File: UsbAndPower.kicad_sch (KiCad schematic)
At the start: 16 parts, among them J4 USB_C_Receptacle_USB2.0_16P, Q4 ZXMN3A14F, Q6 DMG2301L, U4 LM1117MP-3.3, U5 HT75xx-1-SOT89

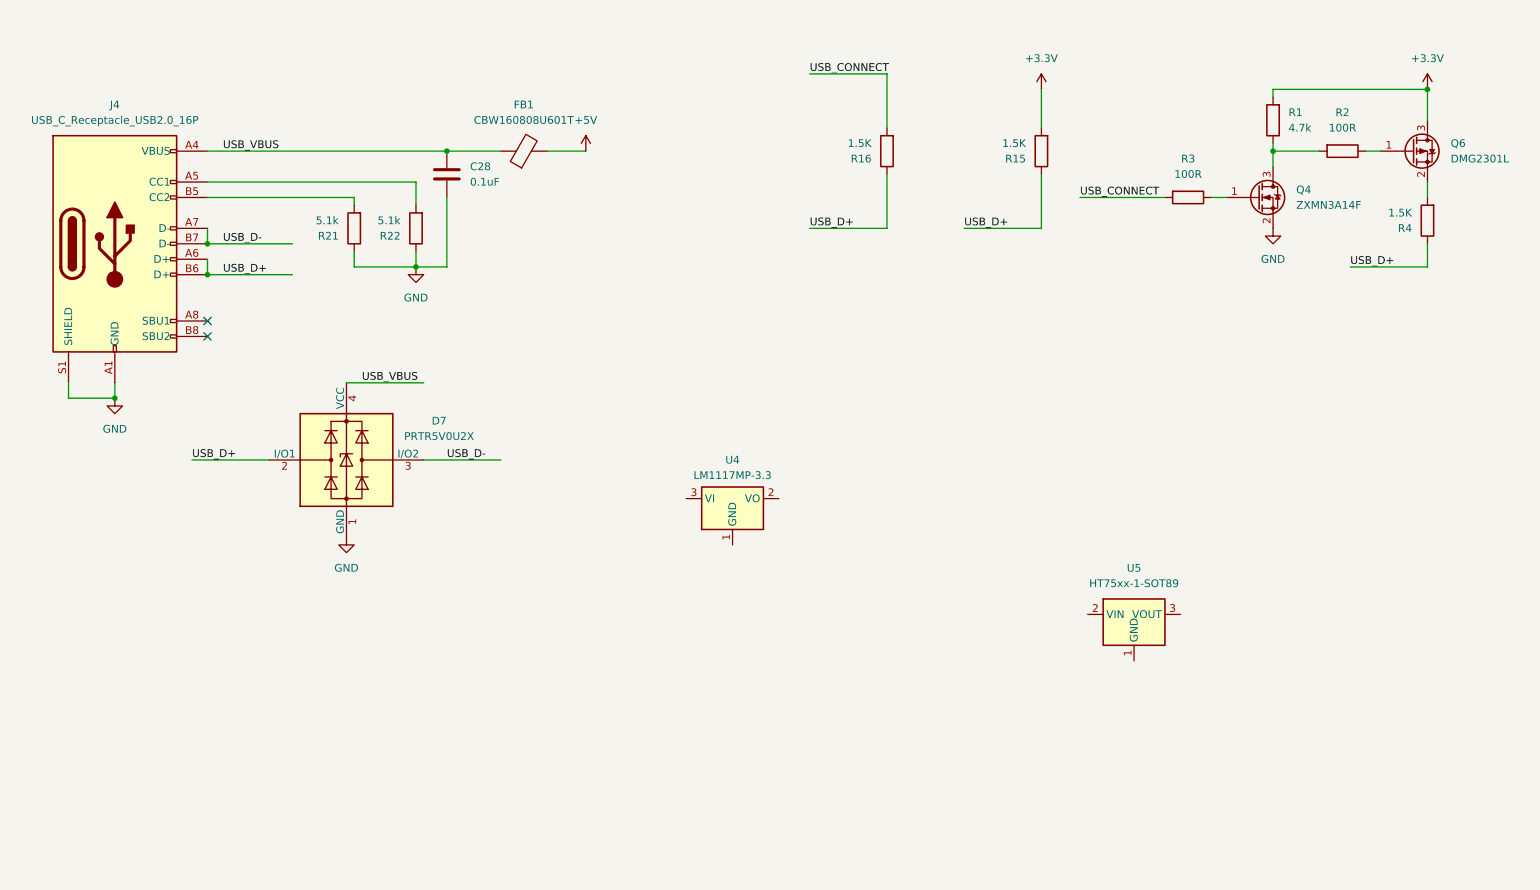
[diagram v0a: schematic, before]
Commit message: 3.3v power ok
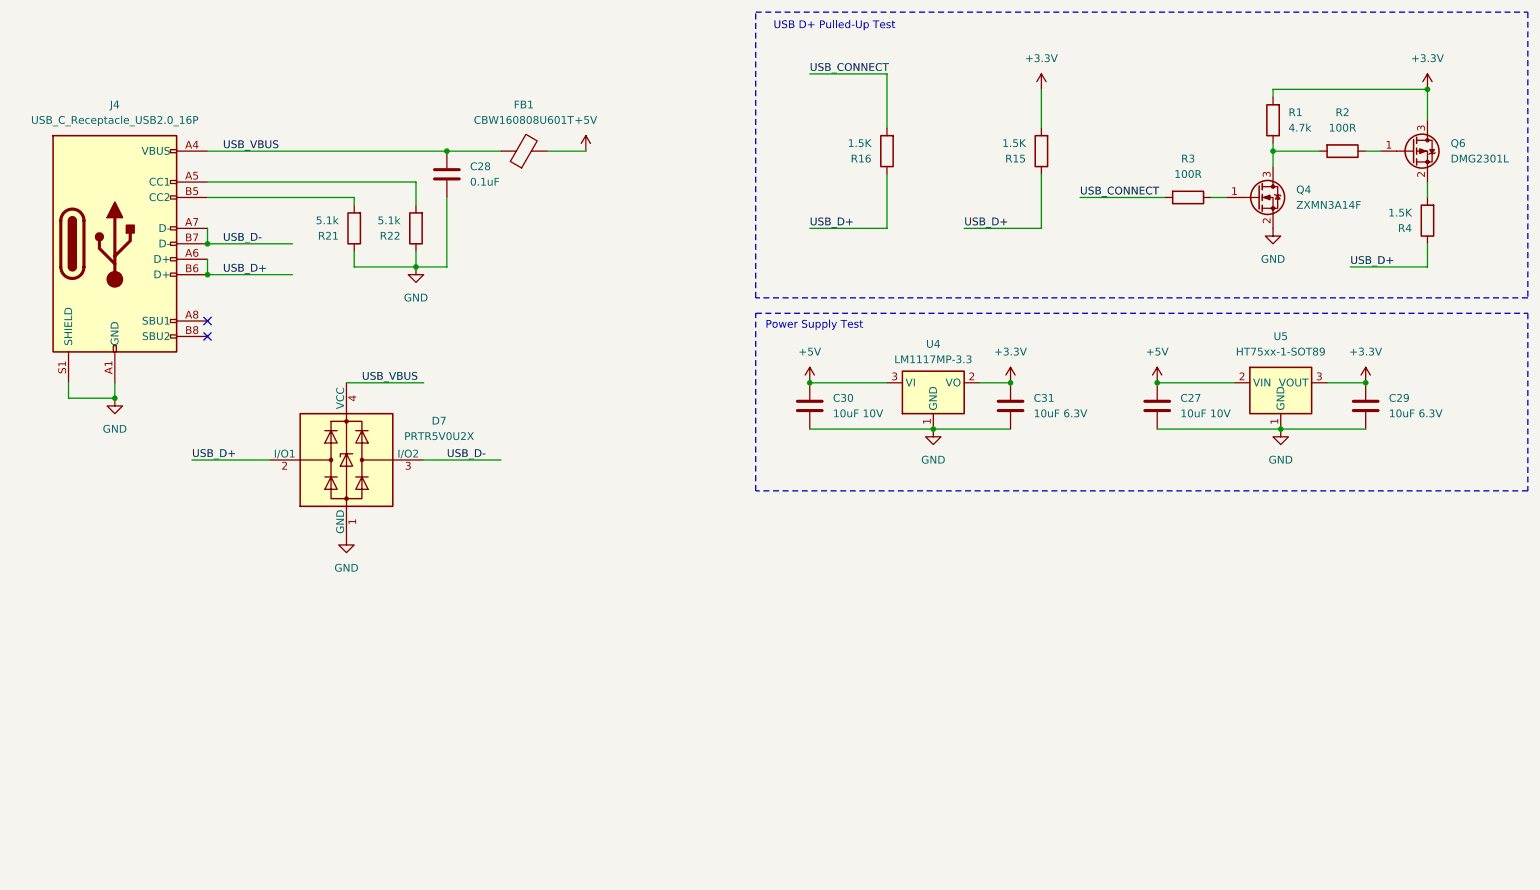
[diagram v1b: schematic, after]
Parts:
- added C27, C30: 10uF 10V, Capacitor_SMD:C_0805_2012Metric, symbol Device:C
- added C29, C31: 10uF 6.3V, Capacitor_SMD:C_0805_2012Metric, symbol Device:C
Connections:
- net +3.3V: now also U4.2 (VO), U5.3 (VOUT), C29.1, C31.1
- net +5V: now also U4.3 (VI), U5.2 (VIN), C27.1, C30.1
- net GND: now also U4.1 (GND), U5.1 (GND), C27.2, C29.2, C30.2, C31.2
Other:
- note added: "Power Supply Test"
- note added: "USB D+ Pulled-Up Test"
- moved on the sheet: U4, U5

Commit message: temp
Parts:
- added C32: 10uF 10V, Capacitor_SMD:C_0805_2012Metric, symbol Device:C
- added U6: RT9193-18GB, Package_TO_SOT_SMD:SOT-23-5, symbol Regulator_Linear:AP131-18
- added U7: RT9193-33GB, Package_TO_SOT_SMD:SOT-23-5, symbol Regulator_Linear:AP131-33
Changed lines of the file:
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@@
+	)
+	(symbol
+		(lib_id "Device:C")
+		(at 147.32 118.11 0)
+		(unit 1)
+		(exclude_from_sim no)
+		(in_bom yes)
+		(on_board yes)
+		(dnp no)
+		(fields_autoplaced yes)
+		(property "Reference" "C32"
+			(at 151.13 116.8399 0)
+			(effects
+				(font
+					(size 1.27 1.27)
+				)
+				(justify left)
+			)
+		)
+		(property "Value" "10uF 10V"
+			(at 151.13 119.3799 0)
+			(effects
+				(font
+					(size 1.27 1.27)
+				)
+				(justify left)
+			)
+		)
+		(property "Footprint" "Capacitor_SMD:C_0805_2012Metric"
+			(at 148.2852 121.92 0)
+			(effects
+				(font
+					(size 1.27 1.27)
+				)
+				(hide yes)
+			)
+		)
+		(property "Datasheet" "~"
+			(at 147.32 118.11 0)
+			(effects
+				(font
+					(size 1.27 1.27)
+				)
+				(hide yes)
+			)
+		)
+		(property "Description" "Unpolarized capacitor"
+			(at 147.32 118.11 0)
+			(effects
+				(font
+					(size 1.27 1.27)
+				)
+				(hide yes)
+			)
+		)
+		(pin "2"
+		)
+		(pin "1"
+		)
+		(instances
+			(project "DapLink_STM32F103CBT6"
+				(path "/62d13f52-5b95-4b2e-9bc7-6f5f907932ec/a477e6ea-0fc3-4cc5-9f90-9fe3a9e18e1a"
+					(reference "C32")
+					(unit 1)
+				)
+			)
+		)
 	)
 	(symbol
@@
 	)
 	(symbol
+		(lib_id "Regulator_Linear:AP131-33")
+		(at 227.33 119.38 0)
+		(unit 1)
+		(exclude_from_sim no)
+		(in_bom yes)
+		(on_board yes)
+		(dnp no)
+		(fields_autoplaced yes)
+		(property "Reference" "U7"
+			(at 227.33 110.49 0)
+			(effects
+				(font
+					(size 1.27 1.27)
+				)
+			)
+		)
+		(property "Value" "RT9193-33GB"
+			(at 227.33 113.03 0)
+			(effects
+				(font
+					(size 1.27 1.27)
+				)
+			)
+		)
+		(property "Footprint" "Package_TO_SOT_SMD:SOT-23-5"
+			(at 227.33 111.125 0)
+			(effects
+				(font
+					(size 1.27 1.27)
+				)
+				(hide yes)
+			)
+		)
+		(property "Datasheet" "https://www.richtek.com/assets/product_file/RT9193/DS9193-18.pdf"
+			(at 227.33 119.38 0)
+			(effects
+				(font
+					(size 1.27 1.27)
+				)
+				(hide yes)
+			)
+		)
+		(property "Description" "300mA, Ultra-Low Noise, Ultra-Fast CMOS LDO Regulator, shutdown pin, 3.3V fixed positive output, SOT-23-5"
+			(at 227.33 119.38 0)
+			(effects
+				(font
+					(size 1.27 1.27)
+				)
+				(hide yes)
+			)
+		)
+		(pin "3"
+		)
+		(pin "1"
+		)
+		(pin "4"
+		)
+		(pin "2"
+		)
+		(pin "5"
+		)
+		(instances
+			(project ""
+				(path "/62d13f52-5b95-4b2e-9bc7-6f5f907932ec/a477e6ea-0fc3-4cc5-9f90-9fe3a9e18e1a"
+					(reference "U7")
+					(unit 1)
+				)
+			)
+		)
+	)
+	(symbol
 		(lib_name "GND_1")
 		(lib_id "power:GND")
@@
 					(unit 1)
 				)
+			)
+		)
+	)
+	(symbol
+		(lib_id "Regulator_Linear:AP131-18")
+		(at 175.26 118.11 0)
+		(unit 1)
+		(exclude_from_sim no)
+		(in_bom yes)
+		(on_board yes)
+		(dnp no)
+		(fields_autoplaced yes)
+		(property "Reference" "U6"
+			(at 175.26 109.22 0)
+			(effects
+				(font
+					(size 1.27 1.27)
+				)
+			)
+		)
+		(property "Value" "RT9193-18GB"
+			(at 175.26 111.76 0)
+			(effects
+				(font
+					(size 1.27 1.27)
+				)
+			)
+		)
+		(property "Footprint" "Package_TO_SOT_SMD:SOT-23-5"
+			(at 175.26 109.855 0)
+			(effects
+				(font
+					(size 1.27 1.27)
+				)
+				(hide yes)
+			)
+		)
+		(property "Datasheet" "https://www.richtek.com/assets/product_file/RT9193/DS9193-18.pdf"
+			(at 175.26 118.11 0)
+			(effects
+				(font
+					(size 1.27 1.27)
+				)
+				(hide yes)
+			)
+		)
+		(property "Description" "300mA, Ultra-Low Noise, Ultra-Fast CMOS LDO Regulator, shutdown pin, 1.8V fixed positive output, SOT-23-5"
+			(at 175.26 118.11 0)
+			(effects
+				(font
+					(size 1.27 1.27)
+				)
+				(hide yes)
+			)
+		)
+		(pin "3"
+		)
+		(pin "4"
+		)
+		(pin "2"
+		)
+		(pin "5"
+		)
+		(pin "1"
+		)
+		(instances
+			(project ""
+				(path "/62d13f52-5b95-4b2e-9bc7-6f5f907932ec/a477e6ea-0fc3-4cc5-9f90-9fe3a9e18e1a"
+					(reference "U6")
+					(unit 1)
+				)

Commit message: temp power
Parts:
- added C33, C35, C37: 1uF 10V X7R, Capacitor_SMD:C_0805_2012Metric, symbol Device:C
- added C34, C36: 22nF, Capacitor_SMD:C_0805_2012Metric, symbol Device:C
- C32: value 10uF 10V -> 1uF 10V X7R
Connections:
- net +3.3V: now also U7.5 (OUT), C37.1
- net +5V: now also C32.1, U6.1 (IN), U6.3 (EN), U7.1 (IN), U7.3 (EN), C35.1
- net GND: now also C32.2, U6.2 (GND), U7.2 (GND), C33.2, C34.2, C35.2, C36.2, C37.2
- net at U7.4 (BP): now also C36.1
- net at U6.4 (BP): now also C34.1
- net +1.8V: now reaches U6.5 (OUT)
- net +1.8V: now also C33.1
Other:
- note added: "Power Supply Test 3.3V"
- note removed: "Power Supply Test"
- moved on the sheet: C32, U6, U7

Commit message: temp
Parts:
- C32, C33, C35, C37: footprint Capacitor_SMD:C_0805_2012Metric -> Capacitor_SMD:C_1206_3216Metric
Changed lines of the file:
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@@
 			)
 		)
-		(property "Footprint" "Capacitor_SMD:C_0805_2012Metric"
+		(property "Footprint" "Capacitor_SMD:C_1206_3216Metric"
 			(at 215.5952 116.84 0)
 			(effects
@@
 			)
 		)
-		(property "Footprint" "Capacitor_SMD:C_0805_2012Metric"
+		(property "Footprint" "Capacitor_SMD:C_1206_3216Metric"
 			(at 215.5952 146.05 0)
 			(effects
@@
 			)
 		)
-		(property "Footprint" "Capacitor_SMD:C_0805_2012Metric"
+		(property "Footprint" "Capacitor_SMD:C_1206_3216Metric"
 			(at 166.0652 116.84 0)
 			(effects
@@
 			)
 		)
-		(property "Footprint" "Capacitor_SMD:C_0805_2012Metric"
+		(property "Footprint" "Capacitor_SMD:C_1206_3216Metric"
 			(at 166.0652 146.05 0)
 			(effects

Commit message: temp
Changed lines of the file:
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@@
-	(wire
-		(pts
-			(xy 80.01 58.42) (xy 66.04 58.42)
-		)
-		(stroke
-			(width 0)
-			(type default)
-		)
-	)
 	(wire
 		(pts
@@
 	(wire
 		(pts
+			(xy 66.04 58.42) (xy 69.85 58.42)
+		)
+		(stroke
+			(width 0)
+			(type default)
+		)
+	)
+	(wire
+		(pts
 			(xy 214.63 116.84) (xy 214.63 121.92)
 		)
@@
 	(wire
 		(pts
-			(xy 80.01 53.34) (xy 66.04 53.34)
-		)
-		(stroke
-			(width 0)
-			(type default)
-		)
-	)
-	(wire
-		(pts
 			(xy 63.5 88.9) (xy 76.2 88.9)
 		)
@@
 		(pts
 			(xy 250.19 76.2) (xy 256.54 76.2)
+		)
+		(stroke
+			(width 0)
+			(type default)
+		)
+	)
+	(wire
+		(pts
+			(xy 66.04 53.34) (xy 69.85 53.34)
 		)
 		(stroke
@@
 		)
 	)
-	(label "USB_D+"
-		(at 68.58 58.42 0)
-		(fields_autoplaced yes)
-		(effects
-			(font
-				(size 1.27 1.27)
-			)
-			(justify left bottom)
-		)
-	)
 	(label "USB_CONNECT"
 		(at 165.1 25.4 0)
@@
 		)
 	)
-	(label "USB_D-"
-		(at 68.58 53.34 0)
-		(fields_autoplaced yes)
-		(effects
-			(font
-				(size 1.27 1.27)
-			)
-			(justify left bottom)
-		)
-	)
 	(label "USB_VBUS"
 		(at 91.44 76.2 0)
@@
 		)
 	)
+	(hierarchical_label "USB_D-"
+		(shape bidirectional)
+		(at 69.85 53.34 0)
+		(fields_autoplaced yes)
+		(effects
+			(font
+				(size 1.27 1.27)
+			)
+			(justify left)
+		)
+	)
+	(hierarchical_label "USB_D+"
+		(shape bidirectional)
+		(at 69.85 58.42 0)
+		(fields_autoplaced yes)
+		(effects
+			(font
+				(size 1.27 1.27)
+			)
+			(justify left)
+		)
+	)

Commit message: temp
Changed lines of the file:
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@@
 	(wire
 		(pts
-			(xy 209.55 45.72) (xy 223.52 45.72)
+			(xy 220.98 45.72) (xy 223.52 45.72)
 		)
 		(stroke
@@
 		)
 	)
-	(label "USB_CONNECT"
-		(at 209.55 45.72 0)
-		(fields_autoplaced yes)
-		(effects
-			(font
-				(size 1.27 1.27)
-			)
-			(justify left bottom)
-		)
-	)
 	(label "USB_D-"
 		(at 105.41 88.9 0)
@@
 		)
 	)
+	(hierarchical_label "USB_CONNECT"
+		(shape input)
+		(at 220.98 45.72 180)
+		(fields_autoplaced yes)
+		(effects
+			(font
+				(size 1.27 1.27)
+			)
+			(justify right)
+		)
+	)

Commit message: temp
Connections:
- net +3.3V: now also Q6.2 (S); no longer C37.1, Q6.3 (D), U7.5 (OUT)
- net at R4.2: now also Q6.3 (D); no longer Q6.2 (S)
- net +1.8V renamed +1.8V_LDO
- new net +3.3V_LDO: C37.1, U7.5 (OUT)
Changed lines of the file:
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@@
+	(wire
+		(pts
+			(xy 177.8 27.94) (xy 177.8 34.29)
+		)
+		(stroke
+			(width 0)
+			(type default)
+		)
+	)
 	(wire
 		(pts
@@
 	(wire
 		(pts
+			(xy 165.1 27.94) (xy 177.8 27.94)
+		)
+		(stroke
+			(width 0)
+			(type default)
+		)
+	)
+	(wire
+		(pts
 			(xy 165.1 121.92) (xy 193.04 121.92)
 		)
@@
 	(wire
 		(pts
-			(xy 165.1 25.4) (xy 177.8 25.4)
-		)
-		(stroke
-			(width 0)
-			(type default)
-		)
-	)
-	(wire
-		(pts
 			(xy 250.19 76.2) (xy 256.54 76.2)
 		)
@@
 	(wire
 		(pts
-			(xy 177.8 25.4) (xy 177.8 34.29)
-		)
-		(stroke
-			(width 0)
-			(type default)
-		)
-	)
-	(wire
-		(pts
 			(xy 241.3 27.94) (xy 266.7 27.94)
 		)
@@
 	(wire
 		(pts
-			(xy 121.92 38.1) (xy 128.27 38.1)
+			(xy 121.92 38.1) (xy 130.81 38.1)
 		)
 		(stroke
@@
 		)
 	)
-	(label "USB_D+"
-		(at 63.5 88.9 0)
+	(label "USB_CONNECT"
+		(at 165.1 27.94 0)
 		(fields_autoplaced yes)
 		(effects
@@
 		)
 	)
-	(label "USB_D-"
-		(at 105.41 88.9 0)
+	(label "USB_D+"
+		(at 63.5 88.9 0)
 		(fields_autoplaced yes)
 		(effects
@@
 		)
 	)
-	(label "USB_CONNECT"
-		(at 165.1 25.4 0)
+	(label "USB_D-"
+		(at 105.41 88.9 0)
 		(fields_autoplaced yes)
 		(effects
@@
 			)
 		)
-		(property "Value" "+3.3V"
+		(property "Value" "+3.3V_LDO"
 			(at 214.63 133.35 0)
 			(effects
@@
 		(on_board yes)
 		(dnp no)
-		(fields_autoplaced yes)
 		(property "Reference" "FB1"
 			(at 118.0592 30.48 90)
@@
 		(lib_id "Transistor_FET:DMG2301L")
 		(at 264.16 38.1 0)
-		(unit 1)
-		(exclude_from_sim no)
-		(in_bom yes)
-		(on_board yes)
-		(dnp no)
-		(fields_autoplaced yes)
+		(mirror x)
+		(unit 1)
+		(exclude_from_sim no)
+		(in_bom yes)
+		(on_board yes)
+		(dnp no)
 		(property "Reference" "Q6"
-			(at 270.51 36.8299 0)
+			(at 270.51 39.3701 0)
 			(effects
 				(font
@@
 		)
 		(property "Value" "DMG2301L"
-			(at 270.51 39.3699 0)
+			(at 270.51 36.8301 0)
 			(effects
 				(font
@@
 		)
 		(property "Footprint" "Package_TO_SOT_SMD:SOT-23"
-			(at 269.24 40.005 0)
+			(at 269.24 36.195 0)
 			(effects
 				(font
@@
 		)
 		(property "Datasheet" "https://www.diodes.com/assets/Datasheets/DMG2301L.pdf"
-			(at 269.24 41.91 0)
+			(at 269.24 34.29 0)
 			(effects
 				(font
@@
 	(symbol
 		(lib_id "power:+5V")
-		(at 128.27 38.1 0)
+		(at 130.81 38.1 0)
 		(unit 1)
 		(exclude_from_sim no)
@@
 		(fields_autoplaced yes)
 		(property "Reference" "#PWR071"
-			(at 128.27 41.91 0)
+			(at 130.81 41.91 0)
 			(effects
 				(font
@@
 		)
 		(property "Value" "+5V"
-			(at 128.27 33.02 0)
+			(at 130.81 33.02 0)
 			(effects
 				(font
@@
 		)
 		(property "Footprint" ""
-			(at 128.27 38.1 0)
+			(at 130.81 38.1 0)
 			(effects
 				(font
@@
 		)
 		(property "Datasheet" ""
-			(at 128.27 38.1 0)
+			(at 130.81 38.1 0)
 			(effects
 				(font
@@
 		)
 		(property "Description" "Power symbol creates a global label with name \"+5V\""
-			(at 128.27 38.1 0)
+			(at 130.81 38.1 0)
 			(effects
 				(font
@@
 			)
 		)
-		(property "Value" "+1.8V"
+		(property "Value" "+1.8V_LDO"
 			(at 214.63 104.14 0)
 			(effects

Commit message: temp
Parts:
- removed Q6: DMG2301L, Package_TO_SOT_SMD:SOT-23, symbol Transistor_FET:DMG2301L
- added Q5: SI2301, Package_TO_SOT_SMD:SOT-23, symbol Transistor_FET:DMG2301L
- Q4: value ZXMN3A14F -> SI2306
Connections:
- net +3.3V: now also Q5.2 (S)
- net at R2.1: now also Q5.1 (G)
- net at R4.2: now also Q5.3 (D)
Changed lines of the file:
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@@
+	)
+	(symbol
+		(lib_id "Transistor_FET:DMG2301L")
+		(at 264.16 38.1 0)
+		(mirror x)
+		(unit 1)
+		(exclude_from_sim no)
+		(in_bom yes)
+		(on_board yes)
+		(dnp no)
+		(property "Reference" "Q5"
+			(at 270.51 39.3701 0)
+			(effects
+				(font
+					(size 1.27 1.27)
+				)
+				(justify left)
+			)
+		)
+		(property "Value" "SI2301"
+			(at 270.51 36.8301 0)
+			(effects
+				(font
+					(size 1.27 1.27)
+				)
+				(justify left)
+			)
+		)
+		(property "Footprint" "Package_TO_SOT_SMD:SOT-23"
+			(at 269.24 36.195 0)
+			(effects
+				(font
+					(size 1.27 1.27)
+					(italic yes)
+				)
+				(justify left)
+				(hide yes)
+			)
+		)
+		(property "Datasheet" "https://www.mccsemi.com/pdf/Products/SI2301(SOT-23).pdf"
+			(at 269.24 34.29 0)
+			(effects
+				(font
+					(size 1.27 1.27)
+				)
+				(justify left)
+				(hide yes)
+			)
+		)
+		(property "Description" "-2.8A Id, -20V Vds, +-8V Vgs, Rds 50mR, P-Channel MOSFET, SOT-23"
+			(at 264.16 38.1 0)
+			(effects
+				(font
+					(size 1.27 1.27)
+				)
+				(hide yes)
+			)
+		)
+		(pin "2"
+		)
+		(pin "1"
+		)
+		(pin "3"
+		)
+		(instances
+			(project "DapLink_STM32F103CBT6"
+				(path "/62d13f52-5b95-4b2e-9bc7-6f5f907932ec/a477e6ea-0fc3-4cc5-9f90-9fe3a9e18e1a"
+					(reference "Q5")
+					(unit 1)
+				)
+			)
+		)
 	)
 	(symbol
@@
 	)
 	(symbol
-		(lib_id "Transistor_FET:DMG2301L")
-		(at 264.16 38.1 0)
-		(mirror x)
-		(unit 1)
-		(exclude_from_sim no)
-		(in_bom yes)
-		(on_board yes)
-		(dnp no)
-		(property "Reference" "Q6"
-			(at 270.51 39.3701 0)
-			(effects
-				(font
-					(size 1.27 1.27)
-				)
-				(justify left)
-			)
-		)
-		(property "Value" "DMG2301L"
-			(at 270.51 36.8301 0)
-			(effects
-				(font
-					(size 1.27 1.27)
-				)
-				(justify left)
-			)
-		)
-		(property "Footprint" "Package_TO_SOT_SMD:SOT-23"
-			(at 269.24 36.195 0)
-			(effects
-				(font
-					(size 1.27 1.27)
-					(italic yes)
-				)
-				(justify left)
-				(hide yes)
-			)
-		)
-		(property "Datasheet" "https://www.diodes.com/assets/Datasheets/DMG2301L.pdf"
-			(at 269.24 34.29 0)
-			(effects
-				(font
-					(size 1.27 1.27)
-				)
-				(justify left)
-				(hide yes)
-			)
-		)
-		(property "Description" "-3A Id, -20V Vds, P-Channel MOSFET, SOT-23"
-			(at 264.16 38.1 0)
-			(effects
-				(font
-					(size 1.27 1.27)
-				)
-				(hide yes)
-			)
-		)
-		(pin "2"
-		)
-		(pin "1"
-		)
-		(pin "3"
-		)
-		(instances
-			(project ""
-				(path "/62d13f52-5b95-4b2e-9bc7-6f5f907932ec/a477e6ea-0fc3-4cc5-9f90-9fe3a9e18e1a"
-					(reference "Q6")
-					(unit 1)
-				)
-			)
-		)
-	)
-	(symbol
 		(lib_name "GND_1")
 		(lib_id "power:GND")
@@
 	)
 	(symbol
-		(lib_id "Transistor_FET:ZXMN3A14F")
-		(at 238.76 45.72 0)
-		(unit 1)
-		(exclude_from_sim no)
-		(in_bom yes)
-		(on_board yes)
-		(dnp no)
-		(property "Reference" "Q4"
-			(at 245.11 44.4499 0)
-			(effects
-				(font
-					(size 1.27 1.27)
-				)
-				(justify left)
-			)
-		)
-		(property "Value" "ZXMN3A14F"
-			(at 245.11 46.9899 0)
-			(effects
-				(font
-					(size 1.27 1.27)
-				)
-				(justify left)
-			)
-		)
-		(property "Footprint" "Package_TO_SOT_SMD:SOT-23"
-			(at 243.84 47.625 0)
-			(effects
-				(font
-					(size 1.27 1.27)
-					(italic yes)
-				)
-				(justify left)
-				(hide yes)
-			)
-		)
-		(property "Datasheet" "http://www.diodes.com/assets/Datasheets/ZXMN3A14F.pdf"
-			(at 243.84 49.53 0)
-			(effects
-				(font
-					(size 1.27 1.27)
-				)
-				(justify left)
-				(hide yes)
-			)
-		)
-		(property "Description" "3.2A Id, 30V Vds, N-Channel MOSFET, SOT-23"
-			(at 238.76 45.72 0)
-			(effects
-				(font
-					(size 1.27 1.27)
-				)
-				(hide yes)
-			)
-		)
-		(pin "1"
-		)
-		(pin "3"
-		)
-		(pin "2"
-		)
-		(instances
-			(project ""
-				(path "/62d13f52-5b95-4b2e-9bc7-6f5f907932ec/a477e6ea-0fc3-4cc5-9f90-9fe3a9e18e1a"
-					(reference "Q4")
-					(unit 1)
-				)
-			)
-		)
-	)
-	(symbol
 		(lib_id "Device:C")
 		(at 198.12 80.01 0)
@@
 					(unit 1)
 				)
+			)
+		)
+	)
+	(symbol
+		(lib_id "Transistor_FET:ZXMN3A14F")
+		(at 238.76 45.72 0)
+		(unit 1)
+		(exclude_from_sim no)
+		(in_bom yes)
+		(on_board yes)
+		(dnp no)
+		(property "Reference" "Q4"
+			(at 245.11 44.4499 0)
+			(effects
+				(font
+					(size 1.27 1.27)
+				)
+				(justify left)
+			)
+		)
+		(property "Value" "SI2306"
+			(at 245.11 46.9899 0)
+			(effects
+				(font
+					(size 1.27 1.27)
+				)
+				(justify left)
+			)
+		)
+		(property "Footprint" "Package_TO_SOT_SMD:SOT-23"
+			(at 243.84 47.625 0)
+			(effects
+				(font
+					(size 1.27 1.27)
+					(italic yes)
+				)
+				(justify left)
+				(hide yes)
+			)
+		)
+		(property "Datasheet" "https://www.mccsemi.com/pdf/Products/SI2306(SOT-23).pdf"
+			(at 243.84 49.53 0)
+			(effects
+				(font
+					(size 1.27 1.27)
+				)
+				(justify left)
+				(hide yes)
+			)
+		)
+		(property "Description" "3.16A Id, 30V Vds, +-20V Vgs, Rds 38mR N-Channel MOSFET, SOT-23"
+			(at 238.76 45.72 0)
+			(effects
+				(font
+					(size 1.27 1.27)
+				)
+				(hide yes)
+			)
+		)
+		(pin "1"
+		)
+		(pin "3"
+		)
+		(pin "2"
+		)
+		(instances
+			(project "DapLink_STM32F103CBT6"
+				(path "/62d13f52-5b95-4b2e-9bc7-6f5f907932ec/a477e6ea-0fc3-4cc5-9f90-9fe3a9e18e1a"
+					(reference "Q4")
+					(unit 1)
+				)
